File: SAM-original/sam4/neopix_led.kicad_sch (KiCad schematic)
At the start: 6 parts, among them J10 Conn_01x04_Socket, J11 Conn_01x04_Socket, J12 Conn_01x04_Socket, J13 Conn_01x04_Socket, J9 Conn_01x04_Socket, U8 SN74LV1T34DBV

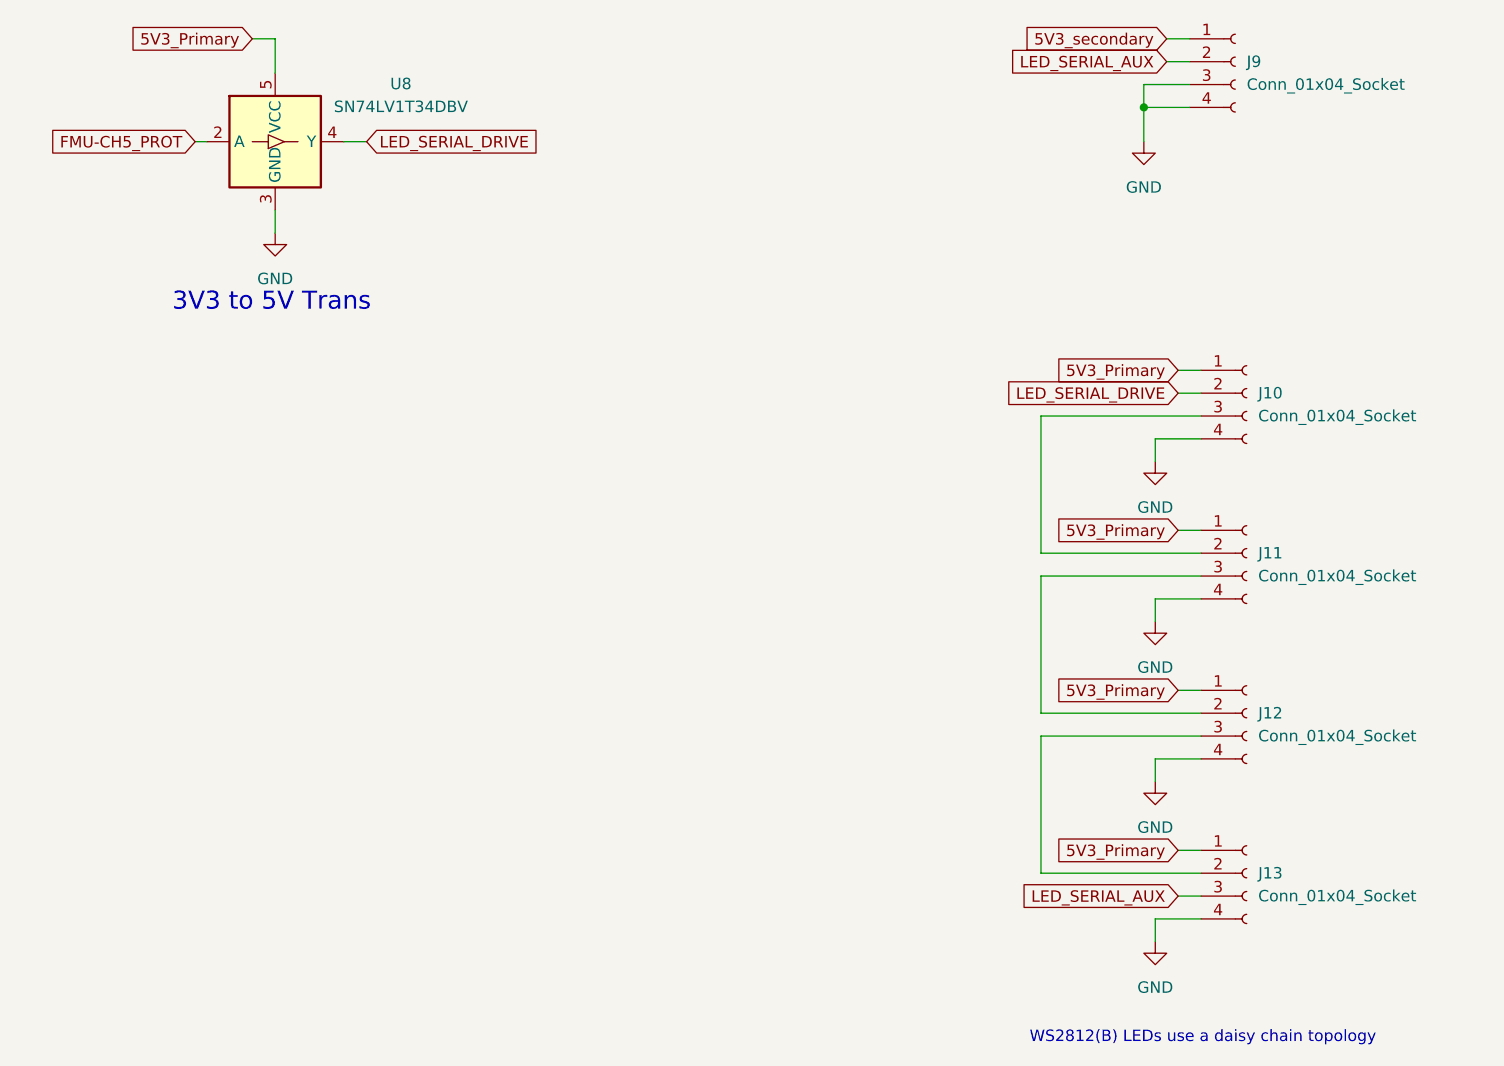
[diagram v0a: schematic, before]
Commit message: reannotate sam schem to bring into parity
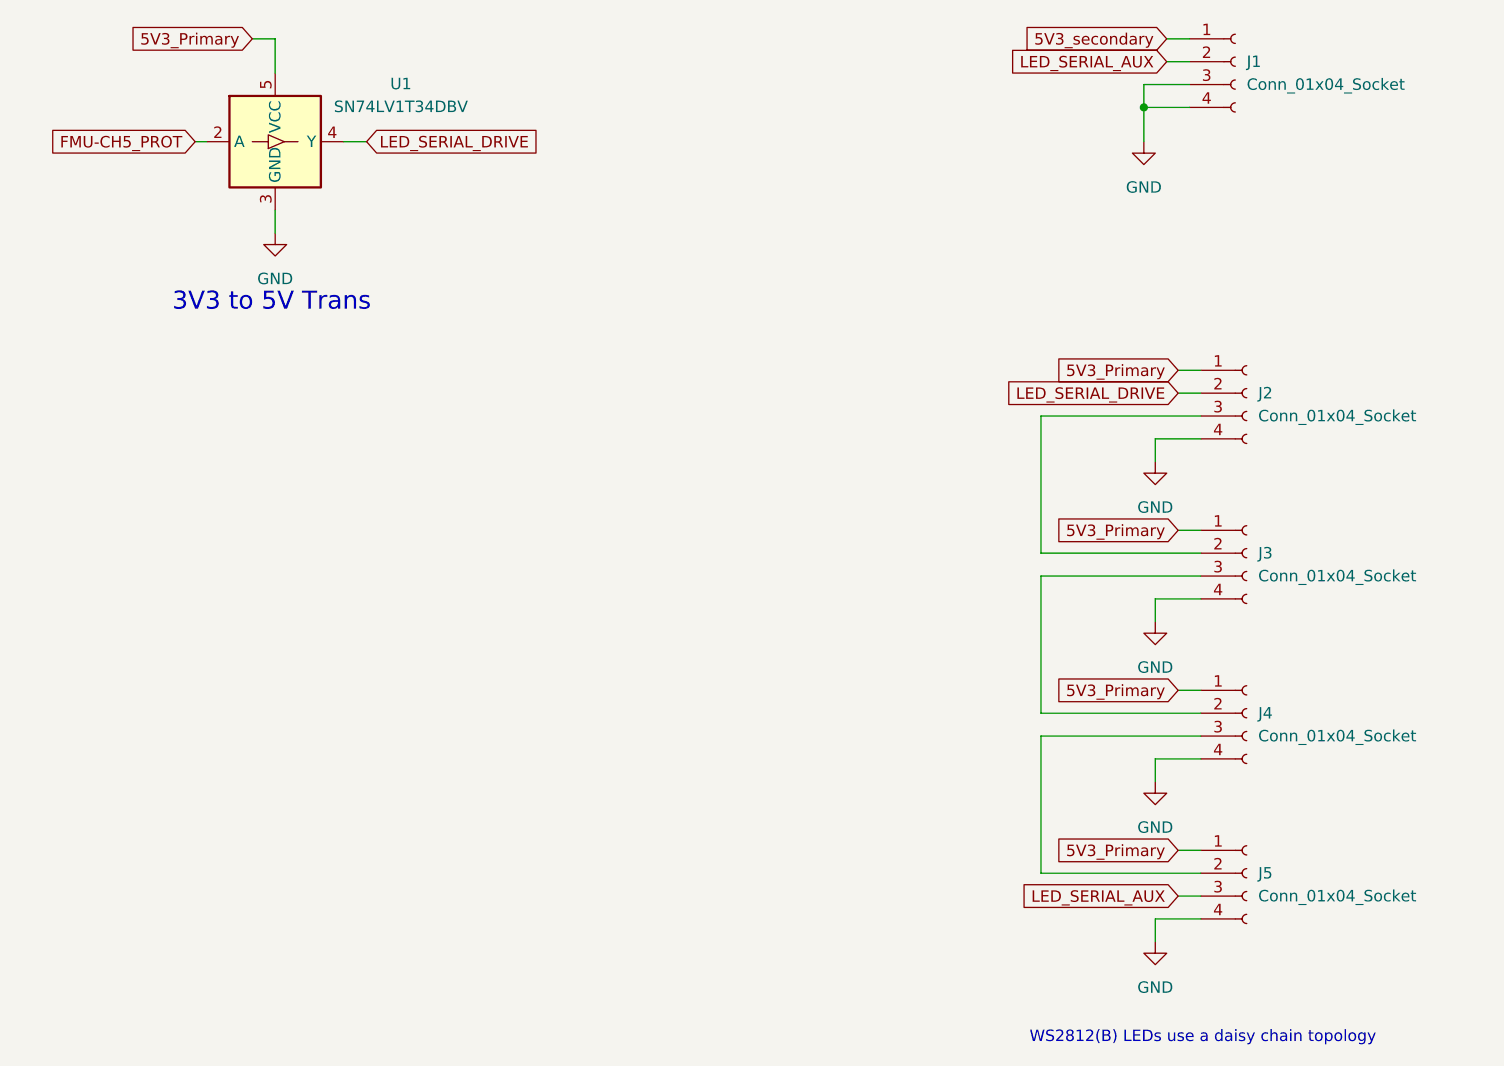
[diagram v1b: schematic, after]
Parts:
- renumbered J9 to J1, J10 to J2, J11 to J3, J12 to J4, J13 to J5, U8 to U1
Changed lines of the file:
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@@
 		(dnp no)
 		(fields_autoplaced yes)
-		(property "Reference" "J9"
+		(property "Reference" "J1"
 			(at 157.48 31.7499 0)
 			(effects
@@
 			(project ""
 				(path "/01aa8038-f16d-42dc-9377-7a3d64116781/fd124b27-45e9-4927-952b-f3813b51cc55"
-					(reference "J9")
+					(reference "J1")
 					(unit 1)
 				)
@@
 		(dnp no)
 		(fields_autoplaced yes)
-		(property "Reference" "J12"
+		(property "Reference" "J4"
 			(at 158.75 104.1399 0)
 			(effects
@@
 			(project "sam4"
 				(path "/01aa8038-f16d-42dc-9377-7a3d64116781/fd124b27-45e9-4927-952b-f3813b51cc55"
-					(reference "J12")
+					(reference "J4")
 					(unit 1)
 				)
@@
 		(on_board yes)
 		(dnp no)
-		(property "Reference" "J11"
+		(property "Reference" "J3"
 			(at 158.75 86.3599 0)
 			(effects
@@
 			(project "sam4"
 				(path "/01aa8038-f16d-42dc-9377-7a3d64116781/fd124b27-45e9-4927-952b-f3813b51cc55"
-					(reference "J11")
+					(reference "J3")
 					(unit 1)
 				)
@@
 		(dnp no)
 		(fields_autoplaced yes)
-		(property "Reference" "J13"
+		(property "Reference" "J5"
 			(at 158.75 121.9199 0)
 			(effects
@@
 			(project "sam4"
 				(path "/01aa8038-f16d-42dc-9377-7a3d64116781/fd124b27-45e9-4927-952b-f3813b51cc55"
-					(reference "J13")
+					(reference "J5")
 					(unit 1)
 				)
@@
 		(on_board yes)
 		(dnp no)
-		(property "Reference" "J10"
+		(property "Reference" "J2"
 			(at 158.75 68.5799 0)
 			(effects
@@
 			(project "sam4"
 				(path "/01aa8038-f16d-42dc-9377-7a3d64116781/fd124b27-45e9-4927-952b-f3813b51cc55"
-					(reference "J10")
+					(reference "J2")
 					(unit 1)
 				)
@@
 		(dnp no)
 		(fields_autoplaced yes)
-		(property "Reference" "U8"
+		(property "Reference" "U1"
 			(at 63.5 34.2198 0)
 			(effects
@@
 			(project ""
 				(path "/01aa8038-f16d-42dc-9377-7a3d64116781/fd124b27-45e9-4927-952b-f3813b51cc55"
-					(reference "U8")
-					(unit 1)
-				)
+					(reference "U1")
+					(unit 1)
+				)

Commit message: add updated SAM4 routing (DRC clean) + model
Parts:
- removed J1, J2, J3, J4, J5: Conn_01x04_Socket, Connector_JST:JST_GH_BM04B-GHS-TBT_1x04-1MP_P1.25mm_Vertical, symbol Connector:Conn_01x04_Socket
- removed U1: SN74LV1T34DBV, Package_TO_SOT_SMD:SOT-23-5, symbol Logic_LevelTranslator:SN74LV1T34DBV
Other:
- note removed: "3V3 to 5V Trans"
- note removed: "WS2812(B) LEDs use a daisy chain topology"
